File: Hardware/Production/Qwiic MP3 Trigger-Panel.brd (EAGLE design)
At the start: 249.7 x 115.8 mm, 1622 parts, among them J1 MICRO-SD, J104 MICRO-SD, J105 ISP, J106 Poke-Home, J107 3.5mm Audio, J110 PTH, J116 MICRO-SD, J117 ISP, J118 Poke-Home, J119 3.5mm Audio, J122 PTH, J128 MICRO-SD, J129 ISP, J13 PTH, J130 Poke-Home, J131 3.5mm Audio, J134 PTH, J140 MICRO-SD, J141 ISP, J142 Poke-Home, J143 3.5mm Audio, J146 PTH, J152 MICRO-SD, J153 ISP, J154 Poke-Home, J155 3.5mm Audio, J158 PTH, J164 MICRO-SD, J165 ISP, J166 Poke-Home, J167 3.5mm Audio, J170 PTH, J176 MICRO-SD, J177 ISP, J178 Poke-Home, J179 3.5mm Audio, J182 PTH, J188 MICRO-SD, J189 ISP, J190 Poke-Home, J191 3.5mm Audio, J20 MICRO-SD, J21 ISP, J22 Poke-Home, J23 3.5mm Audio, J26 PTH, J3 PTH, J32 MICRO-SD, J33 ISP, J34 Poke-Home, J35 3.5mm Audio, J38 PTH, J44 MICRO-SD, J45 ISP, J46 Poke-Home, J47 3.5mm Audio, J50 PTH, J56 MICRO-SD, J57 ISP, J58 Poke-Home, J59 3.5mm Audio, J62 PTH, J68 MICRO-SD, J69 ISP, J7 ISP, J70 Poke-Home, J71 3.5mm Audio, J74 PTH, J8 3.5mm Audio, J80 MICRO-SD, J81 ISP, J82 Poke-Home, J83 3.5mm Audio, J86 PTH, J9 Poke-Home, J92 MICRO-SD, J93 ISP, J94 Poke-Home, J95 3.5mm Audio, J98 PTH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

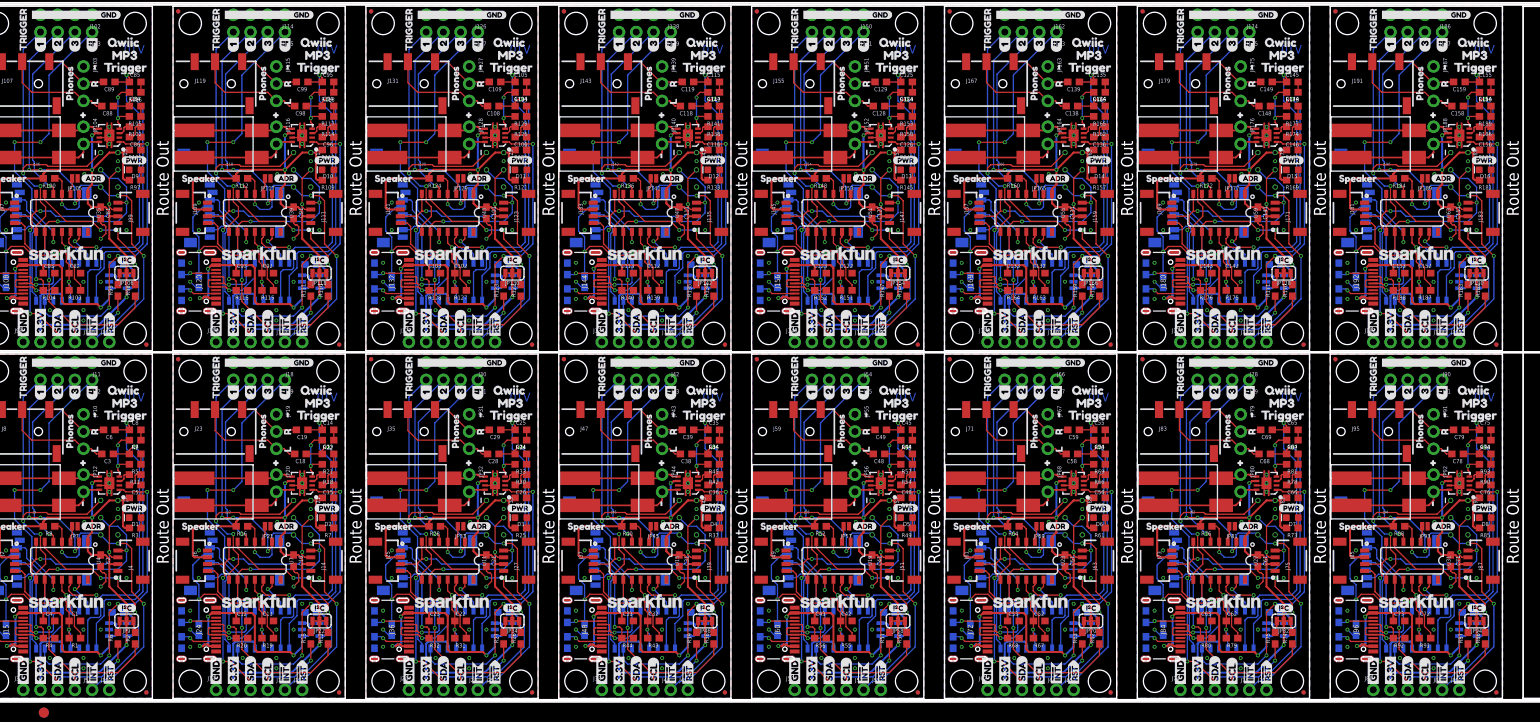
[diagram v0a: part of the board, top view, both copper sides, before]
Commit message: Adding production panel files for v11 reds
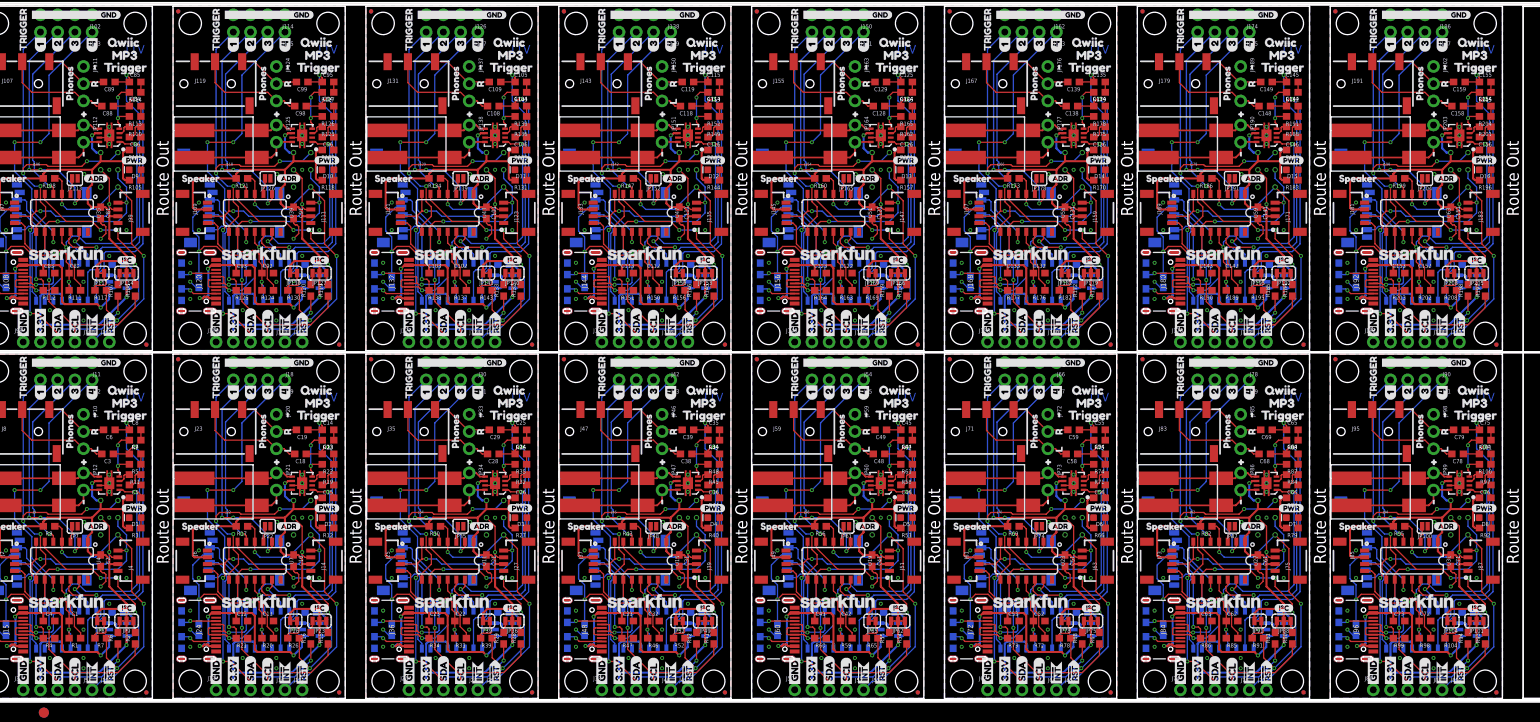
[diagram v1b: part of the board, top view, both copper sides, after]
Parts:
- added JP193, JP194, JP196, JP197, JP206, JP207: STAND-OFF, SparkFun:STAND-OFF
- added JP195, JP208: INT, SparkFun-Jumpers:SMT-JUMPER_2_NC_TRACE_SILK
- added JP198, JP199, JP200, JP201: FIDUCIALUFIDUCIAL, SparkFun:MICRO-FIDUCIAL
- added JP202: PTH, SparkFun-Connectors:1X03_NO_SILK
- added JP203: PTH, SparkFun-Connectors:1X02_NO_SILK
- added JP204: ADR, SparkFun-Jumpers:SMT-JUMPER_2_NO_SILK
- added JP205: (no value), SparkFun-Jumpers:SMT-JUMPER_3_2-NC_TRACE_SILK
- added R193, R194, R206, R207: 5.1k, SparkFun-Resistors:0603
- added R195, R200, R202, R204, R205, R208: 10k, SparkFun-Resistors:0603
- added R196: 1k, SparkFun-Resistors:0603
- added R197, R198, R203: 2.2k, SparkFun-Resistors:0603
- added R199: 4.7k, SparkFun-Resistors:0603
- added R201: 100k, SparkFun-Resistors:0603
- JP100, JP113, JP126, JP87: value FIDUCIALUFIDUCIAL -> ADR; device SparkFun:MICRO-FIDUCIAL -> SparkFun-Jumpers:SMT-JUMPER_2_NO_SILK
- JP101, JP114, JP75, JP88: value FIDUCIALUFIDUCIAL -> (none); device SparkFun:MICRO-FIDUCIAL -> SparkFun-Jumpers:SMT-JUMPER_3_2-NC_TRACE_SILK
- JP102, JP15, JP171, JP183, JP184, JP27, JP28, JP40, JP41, JP51, JP53, JP54, JP63, JP64, JP66, JP76, JP77, JP89, JP90: value FIDUCIALUFIDUCIAL -> STAND-OFF; device SparkFun:MICRO-FIDUCIAL -> SparkFun:STAND-OFF
- JP103, JP115, JP67, JP79: value PTH -> STAND-OFF; device SparkFun-Connectors:1X03_NO_SILK -> SparkFun:STAND-OFF
- JP104: value PTH -> INT; device SparkFun-Connectors:1X02_NO_SILK -> SparkFun-Jumpers:SMT-JUMPER_2_NC_TRACE_SILK
- JP105, JP129, JP141, JP93: value ADR -> STAND-OFF; device SparkFun-Jumpers:SMT-JUMPER_2_NO_NO-SILK -> SparkFun:STAND-OFF
- JP106, JP118, JP142, JP154: value (none) -> STAND-OFF; device SparkFun-Jumpers:SMT-JUMPER_3_2-NC_TRACE_SILK -> SparkFun:STAND-OFF
- JP107, JP108, JP109, JP110, JP120, JP121, JP122, JP133, JP134, JP146, JP71, JP83, JP84, JP95, JP96, JP97: value STAND-OFF -> FIDUCIALUFIDUCIAL; device SparkFun:STAND-OFF -> SparkFun:MICRO-FIDUCIAL
- JP111, JP124, JP137, JP150: value FIDUCIALUFIDUCIAL -> PTH; device SparkFun:MICRO-FIDUCIAL -> SparkFun-Connectors:1X03_NO_SILK
- JP112, JP125, JP138, JP99: value FIDUCIALUFIDUCIAL -> PTH; device SparkFun:MICRO-FIDUCIAL -> SparkFun-Connectors:1X02_NO_SILK
- JP116, JP128, JP80, JP92: value PTH -> STAND-OFF; device SparkFun-Connectors:1X02_NO_SILK -> SparkFun:STAND-OFF
- JP117: value ADR -> INT; device SparkFun-Jumpers:SMT-JUMPER_2_NO_NO-SILK -> SparkFun-Jumpers:SMT-JUMPER_2_NC_TRACE_SILK
- JP127: value PTH -> (none); device SparkFun-Connectors:1X03_NO_SILK -> SparkFun-Jumpers:SMT-JUMPER_3_2-NC_TRACE_SILK
- JP130: value (none) -> INT; device SparkFun-Jumpers:SMT-JUMPER_3_2-NC_TRACE_SILK -> SparkFun-Jumpers:SMT-JUMPER_2_NC_TRACE_SILK
- JP139: value PTH -> ADR; device SparkFun-Connectors:1X03_NO_SILK -> SparkFun-Jumpers:SMT-JUMPER_2_NO_SILK
- JP140: value PTH -> (none); device SparkFun-Connectors:1X02_NO_SILK -> SparkFun-Jumpers:SMT-JUMPER_3_2-NC_TRACE_SILK
- JP143, JP156, JP169, JP182, JP26, JP8: value STAND-OFF -> INT; device SparkFun:STAND-OFF -> SparkFun-Jumpers:SMT-JUMPER_2_NC_TRACE_SILK
- JP151: device SparkFun-Connectors:1X03_NO_SILK -> SparkFun-Connectors:1X02_NO_SILK
- JP152: value PTH -> ADR; device SparkFun-Connectors:1X02_NO_SILK -> SparkFun-Jumpers:SMT-JUMPER_2_NO_SILK
- JP153: value ADR -> (none); device SparkFun-Jumpers:SMT-JUMPER_2_NO_NO-SILK -> SparkFun-Jumpers:SMT-JUMPER_3_2-NC_TRACE_SILK
- JP165, JP7: device SparkFun-Jumpers:SMT-JUMPER_2_NO_NO-SILK -> SparkFun-Jumpers:SMT-JUMPER_2_NO_SILK
- JP175, JP187, JP19, JP31, JP43, JP55: value PTH -> FIDUCIALUFIDUCIAL; device SparkFun-Connectors:1X03_NO_SILK -> SparkFun:MICRO-FIDUCIAL
- JP176, JP20: device SparkFun-Connectors:1X02_NO_SILK -> SparkFun-Connectors:1X03_NO_SILK
- JP177, JP21: value ADR -> PTH; device SparkFun-Jumpers:SMT-JUMPER_2_NO_NO-SILK -> SparkFun-Connectors:1X02_NO_SILK
- JP178, JP22: value (none) -> ADR; device SparkFun-Jumpers:SMT-JUMPER_3_2-NC_TRACE_SILK -> SparkFun-Jumpers:SMT-JUMPER_2_NO_SILK
- JP179, JP192, JP23, JP36, JP49, JP62: value STAND-OFF -> (none); device SparkFun:STAND-OFF -> SparkFun-Jumpers:SMT-JUMPER_3_2-NC_TRACE_SILK
- JP188, JP32, JP44, JP56, JP68: value PTH -> FIDUCIALUFIDUCIAL; device SparkFun-Connectors:1X02_NO_SILK -> SparkFun:MICRO-FIDUCIAL
- JP189, JP33: value ADR -> PTH; device SparkFun-Jumpers:SMT-JUMPER_2_NO_NO-SILK -> SparkFun-Connectors:1X03_NO_SILK
- JP190, JP34: value (none) -> PTH; device SparkFun-Jumpers:SMT-JUMPER_3_2-NC_TRACE_SILK -> SparkFun-Connectors:1X02_NO_SILK
- JP191, JP35, JP48, JP61, JP74: value STAND-OFF -> ADR; device SparkFun:STAND-OFF -> SparkFun-Jumpers:SMT-JUMPER_2_NO_SILK
- JP39, JP52, JP65, JP78: value FIDUCIALUFIDUCIAL -> INT; device SparkFun:MICRO-FIDUCIAL -> SparkFun-Jumpers:SMT-JUMPER_2_NC_TRACE_SILK
- JP45, JP57, JP69, JP81: value ADR -> FIDUCIALUFIDUCIAL; device SparkFun-Jumpers:SMT-JUMPER_2_NO_NO-SILK -> SparkFun:MICRO-FIDUCIAL
- JP46: value (none) -> PTH; device SparkFun-Jumpers:SMT-JUMPER_3_2-NC_TRACE_SILK -> SparkFun-Connectors:1X03_NO_SILK
- JP47, JP60, JP73, JP86: value STAND-OFF -> PTH; device SparkFun:STAND-OFF -> SparkFun-Connectors:1X02_NO_SILK
- JP58, JP70, JP82, JP94: value (none) -> FIDUCIALUFIDUCIAL; device SparkFun-Jumpers:SMT-JUMPER_3_2-NC_TRACE_SILK -> SparkFun:MICRO-FIDUCIAL
- JP59, JP72, JP85, JP98: value STAND-OFF -> PTH; device SparkFun:STAND-OFF -> SparkFun-Connectors:1X03_NO_SILK
- JP91: value PTH -> INT; device SparkFun-Connectors:1X03_NO_SILK -> SparkFun-Jumpers:SMT-JUMPER_2_NC_TRACE_SILK
- R100, R124, R148, R52, R88: value 4.7k -> 10k
- R102, R90: value 100k -> 5.1k
- R103, R115, R129, R141, R142, R154, R77, R89: value 10k -> 5.1k
- R104, R111, R122, R135, R140, R152, R176, R182, R20, R26, R39, R44, R62, R74, R75, R87, R98: value 2.2k -> 10k
- R105, R118, R53, R79: value 10k -> 1k
- R106, R125, R151, R177, R185, R190, R21, R29, R34, R41, R55, R67, R81, R93, R94: value 10k -> 2.2k
- R107, R119, R120, R132, R47, R60: value 5.1k -> 2.2k
- R108, R95: value 5.1k -> 4.7k
- R109, R169, R49, R61, R7, R85: value 1k -> 10k
- R110, R123, R188, R32: value 2.2k -> 100k
- R112, R16, R172, R184, R28: value 4.7k -> 2.2k
- R114, R126, R150, R174, R18, R78: value 100k -> 10k
- R116, R128, R38, R50, R51, R63: value 2.2k -> 5.1k
- R12, R170, R183, R27, R92: value 2.2k -> 1k
- R121: value 1k -> 4.7k
- R131, R144: value 5.1k -> 1k
- R133, R145, R73: value 1k -> 2.2k
- R134, R147, R56: value 2.2k -> 4.7k
- R136: value 4.7k -> 100k
- R138, R42, R54: value 100k -> 2.2k
- R143, R156, R179, R191, R192, R23, R35, R36, R48, R59, R72, R83, R96: value 5.1k -> 10k
- R149, R175, R19, R45, R58: value 10k -> 100k
- R17, R173, R43, R69, R82: value 10k -> 4.7k
- R181, R25, R37: value 1k -> 5.1k
- R186, R30: value 100k -> 4.7k
- R40: value 4.7k -> 1k
- R64, R76: value 4.7k -> 5.1k
- R66: value 100k -> 1k
- R71, R84: value 5.1k -> 100k
- R97: value 1k -> 100k
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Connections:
- new net N$100: C146.2, R188.1
- new net N$101: C144.2, R191.1
- new net N$102: C145.2, R192.1
- new net N$103: J180.B5, R193.2
- new net N$104: J180.A5, R194.2
- new net N$105: JP195.1, R195.2
- new net N$106: D16.A, R196.1
- new net N$107: C156.2, R201.1
- new net N$108: C154.2, R204.1
- new net N$109: C155.2, R205.1
- new net N$110: J192.B5, R206.2
- new net N$111: J192.A5, R207.2
- new net N$112: JP208.1, R208.2
- new net N$97: J168.A5, R181.2
- new net N$98: JP182.1, R182.2
- new net N$99: D15.A, R183.1
- net !INT: now also R7.1
- net !INT1: now also R26.1
- net !INT10: now also R143.1
- net !INT11: now also R156.1
- net !INT12: now also R169.1
- net !INT13: now also R182.1
- net !INT14: now also R195.1
- net !INT15: now also R208.1
- net !INT2: now also R39.1
- net !INT3: now also R52.1
- net !INT4: now also R65.1
- net !INT5: now also R78.1
- net !INT6: now also R91.1
- net !INT7: now also R104.1
- net !INT8: now also R117.1
- net !INT9: now also R130.1
- net !RST1: now also R17.1; no longer R16.1
- net !RST10: now also R134.1; no longer R124.1
- net !RST11: now also R147.1; no longer R136.1
- net !RST12: now also R160.1; no longer R148.1
- net !RST13: now also R173.1; no longer R160.1
- net !RST14: now also R186.1; no longer R172.1
- net !RST15: now also R199.1; no longer R184.1
- net !RST2: now also R30.1; no longer R28.1
- net !RST3: now also R43.1; no longer R40.1
- net !RST4: now also R56.1; no longer R52.1
- net !RST5: now also R69.1; no longer R64.1
- net !RST6: now also R82.1; no longer R76.1
- net !RST7: now also R95.1; no longer R88.1
- net !RST8: now also R108.1; no longer R100.1
- net !RST9: now also R121.1; no longer R112.1
- net !SDN: no longer R10.1, U1.1
- net !SDN1: no longer R17.1, U6.1
- net !SDN10: no longer R125.1, U42.1
- net !SDN11: no longer R137.1, U46.1
- net !SDN12: no longer R149.1, U50.1
- net !SDN13: no longer R161.1, U54.1
- net !SDN14: no longer R173.1, U58.1
- net !SDN15: no longer R185.1, U62.1
- net !SDN2: no longer R29.1, U10.1
- net !SDN3: no longer R41.1, U14.1
- net !SDN4: no longer R53.1, U18.1
- net !SDN5: no longer R65.1, U22.1
- net !SDN6: no longer R77.1, U26.1
- net !SDN7: no longer R89.1, U30.1
- net !SDN8: no longer R101.1, U34.1
- net !SDN9: no longer R113.1, U38.1
- net 3.3V: now also JP8.2
- net 3.3V1: now also JP23.2, JP26.2, R12.2, R18.2; no longer JP22.2, R16.2, R7.2
- net 3.3V10: now also JP140.2, JP143.2, R131.2, R134.2, R135.2; no longer JP130.2, R121.2, R124.2, R125.2
- net 3.3V11: now also JP153.2, JP156.2, R144.2, R147.2, R148.2; no longer JP142.2, R133.2, R136.2, R137.2
- net 3.3V12: now also JP166.2, JP169.2, R157.2, R160.2, R161.2; no longer JP154.2, R145.2, R148.2, R149.2
- net 3.3V13: now also JP179.2, JP182.2, R170.2, R173.2, R174.2; no longer JP166.2, R157.2, R160.2, R161.2
- net 3.3V14: now also JP192.2, JP195.2, R183.2, R186.2, R187.2; no longer JP178.2, R169.2, R172.2, R173.2
- net 3.3V15: now also JP205.2, JP208.2, R196.2, R199.2, R200.2; no longer JP190.2, R181.2, R184.2, R185.2
- net 3.3V2: now also JP36.2, JP39.2, R27.2, R30.2, R31.2; no longer JP34.2, R25.2, R28.2, R29.2
- net 3.3V3: now also JP49.2, JP52.2, R43.2, R44.2; no longer JP46.2, R37.2, R41.2
- net 3.3V4: now also JP62.2, JP65.2, R56.2, R57.2; no longer JP58.2, R49.2, R52.2
- net 3.3V5: now also JP75.2, JP78.2, R66.2, R69.2, R70.2; no longer JP70.2, R61.2, R64.2, R65.2
- net 3.3V6: now also JP88.2, JP91.2, R79.2, R82.2, R83.2; no longer JP82.2, R73.2, R76.2, R77.2
- net 3.3V7: now also JP101.2, JP104.2, R92.2, R95.2, R96.2; no longer JP94.2, R85.2, R88.2, R89.2
- net 3.3V8: now also JP114.2, JP117.2, R105.2, R108.2, R109.2; no longer JP106.2, R100.2, R101.2, R97.2
- net 3.3V9: now also JP127.2, JP130.2, R118.2, R121.2, R122.2; no longer JP118.2, R109.2, R112.2, R113.2
- net AC-L1: now also JP20.3; no longer JP19.3
- net AC-L10: now also JP137.3; no longer JP127.3
- net AC-L11: now also JP150.3; no longer JP139.3
- net AC-L12: now also JP163.3; no longer JP151.3
- net AC-L13: now also JP176.3; no longer JP163.3
- net AC-L14: now also JP189.3; no longer JP175.3
- net AC-L15: now also JP202.3; no longer JP187.3
- net AC-L2: now also JP33.3; no longer JP31.3
- net AC-L3: now also JP46.3; no longer JP43.3
- net AC-L4: now also JP59.3; no longer JP55.3
- net AC-L5: now also JP72.3; no longer JP67.3
- net AC-L6: now also JP85.3; no longer JP79.3
- net AC-L7: now also JP98.3; no longer JP91.3
- net AC-L8: now also JP111.3; no longer JP103.3
- net AC-L9: now also JP124.3; no longer JP115.3
- net AC-R1: now also JP20.2; no longer JP19.2
- net AC-R10: now also JP137.2; no longer JP127.2
- net AC-R11: now also JP150.2; no longer JP139.2
- net AC-R12: now also JP163.2; no longer JP151.2
- net AC-R13: now also JP176.2; no longer JP163.2
- net AC-R14: now also JP189.2; no longer JP175.2
- net AC-R15: now also JP202.2; no longer JP187.2
- net AC-R2: now also JP33.2; no longer JP31.2
- net AC-R3: now also JP46.2; no longer JP43.2
- net AC-R4: now also JP59.2; no longer JP55.2
- net AC-R5: now also JP72.2; no longer JP67.2
- net AC-R6: now also JP85.2; no longer JP79.2
- net AC-R7: now also JP98.2; no longer JP91.2
- net AC-R8: now also JP111.2; no longer JP103.2
- net AC-R9: now also JP124.2; no longer JP115.2
- net ADKEY1: now also R20.1; no longer R19.1
- net ADKEY10: now also R137.1; no longer R127.1
- net ADKEY11: now also R150.1; no longer R139.1
- net ADKEY12: now also R163.1; no longer R151.1
- net ADKEY13: now also R176.1; no longer R163.1
- net ADKEY14: now also R189.1; no longer R175.1
- net ADKEY15: now also R202.1; no longer R187.1
- net ADKEY2: now also R33.1; no longer R31.1
- net ADKEY3: now also R46.1; no longer R43.1
- net ADKEY4: now also R59.1; no longer R55.1
- net ADKEY5: now also R72.1; no longer R67.1
- net ADKEY6: now also R85.1; no longer R79.1
- net ADKEY7: now also R98.1; no longer R91.1
- net ADKEY8: now also R111.1; no longer R103.1
- net ADKEY9: now also R124.1; no longer R115.1
- net ADR1: now also JP22.2; no longer JP21.2
- net ADR10: now also JP139.2; no longer JP129.2
- net ADR11: now also JP152.2; no longer JP141.2
- net ADR12: now also JP165.2; no longer JP153.2
- net ADR13: now also JP178.2; no longer JP165.2
- net ADR14: now also JP191.2; no longer JP177.2
- net ADR15: now also JP204.2; no longer JP189.2
- net ADR2: now also JP35.2; no longer JP33.2
- net ADR3: now also JP48.2; no longer JP45.2
- net ADR4: now also JP61.2; no longer JP57.2
- net ADR5: now also JP74.2; no longer JP69.2
- net ADR6: now also JP87.2; no longer JP81.2
- net ADR7: now also JP100.2; no longer JP93.2
- net ADR8: now also JP113.2; no longer JP105.2
- net ADR9: now also JP126.2; no longer JP117.2
- net GND1: now also JP20.1, JP22.1, R21.1, R25.1; no longer JP19.1, JP21.1, R20.1, R23.1
- net GND10: now also JP137.1, JP139.1, R138.1, R141.1, R142.1; no longer JP127.1, JP129.1, R128.1, R131.1, R132.1
- net GND11: now also JP150.1, JP152.1, R151.1, R154.1, R155.1; no longer JP139.1, JP141.1, R140.1, R143.1, R144.1
- net GND12: now also JP163.1, JP165.1, R164.1, R167.1, R168.1; no longer JP151.1, JP153.1, R152.1, R155.1, R156.1
- net GND13: now also JP176.1, JP178.1, R177.1, R180.1, R181.1; no longer JP163.1, JP165.1, R164.1, R167.1, R168.1
- net GND14: now also JP189.1, JP191.1, R190.1, R193.1, R194.1; no longer JP175.1, JP177.1, R176.1, R179.1, R180.1
- net GND15: now also JP202.1, JP204.1, R203.1, R206.1, R207.1; no longer JP187.1, JP189.1, R188.1, R191.1, R192.1
- net GND2: now also JP35.1, R34.1, R37.1, R38.1; no longer JP31.1, R32.1, R35.1, R36.1
- net GND3: now also JP46.1, JP48.1, R50.1, R51.1; no longer JP43.1, JP45.1, R44.1, R48.1
- net GND4: now also JP59.1, JP61.1, R63.1, R64.1; no longer JP55.1, JP57.1, R56.1, R59.1
- net GND5: now also JP72.1, JP74.1, R73.1, R76.1, R77.1; no longer JP67.1, JP69.1, R68.1, R71.1, R72.1
- net GND6: now also JP85.1, JP87.1, R86.1, R89.1, R90.1; no longer JP79.1, JP81.1, R80.1, R83.1, R84.1
- net GND7: now also JP100.1, JP98.1, R102.1, R103.1, R99.1; no longer JP91.1, JP93.1, R92.1, R95.1, R96.1
- net GND8: now also JP111.1, JP113.1, R112.1, R115.1, R116.1; no longer JP103.1, JP105.1, R104.1, R107.1, R108.1
- net GND9: now also JP124.1, JP126.1, R125.1, R128.1, R129.1; no longer JP115.1, JP117.1, R116.1, R119.1, R120.1
- net IN+AMP1: now also R19.2; no longer R18.2
- net IN+AMP10: now also R136.2; no longer R126.2
- net IN+AMP11: now also R149.2; no longer R138.2
- net IN+AMP12: now also R162.2; no longer R150.2
- net IN+AMP13: now also R175.2; no longer R162.2
- net IN+AMP14: now also R188.2; no longer R174.2
- net IN+AMP15: now also R201.2; no longer R186.2
- net IN+AMP2: now also R32.2; no longer R30.2
- net IN+AMP3: now also R45.2; no longer R42.2
- net IN+AMP4: now also R58.2; no longer R54.2
- net IN+AMP5: now also R71.2; no longer R66.2
- net IN+AMP6: now also R84.2; no longer R78.2
- net IN+AMP7: now also R97.2; no longer R90.2
- net IN+AMP8: now also R110.2; no longer R102.2
- net IN+AMP9: now also R123.2; no longer R114.2
- net IN-AMP1: now also R23.2; no longer R21.2
- net IN-AMP10: now also R139.2, R140.2; no longer R129.2, R130.2
- net IN-AMP11: now also R152.2, R153.2; no longer R141.2, R142.2
- net IN-AMP12: now also R165.2, R166.2; no longer R153.2, R154.2
- net IN-AMP13: now also R178.2, R179.2; no longer R165.2, R166.2
- net IN-AMP14: now also R191.2, R192.2; no longer R177.2, R178.2
- net IN-AMP15: now also R204.2, R205.2; no longer R189.2, R190.2
- net IN-AMP2: now also R35.2, R36.2; no longer R33.2, R34.2
- net IN-AMP3: now also R48.2, R49.2; no longer R45.2, R46.2
- net IN-AMP4: now also R61.2, R62.2; no longer R57.2, R58.2
- net IN-AMP5: now also R74.2, R75.2; no longer R69.2, R70.2
- net IN-AMP6: now also R87.2, R88.2; no longer R81.2, R82.2
- net IN-AMP7: now also R100.2, R101.2; no longer R93.2, R94.2
- net IN-AMP8: now also R113.2, R114.2; no longer R105.2, R106.2
- net IN-AMP9: now also R126.2, R127.2; no longer R117.2, R118.2
- net N$10: now also C13.2; no longer C14.2
- net N$11: now also C14.2, R23.1; no longer J24.B5, R23.2
- net N$12: now also J24.B5; no longer J24.A5
- net N$13: now also J24.A5, R25.2; no longer D3.A, R25.1
- net N$14: now also JP26.1, R26.2; no longer C26.2, R30.1
- net N$15: now also D3.A, R27.1; no longer C24.2, R33.1
- net N$16: now also C26.2, R32.1; no longer C25.2, R34.1
- net N$17: now also C24.2, R35.1; no longer J36.B5, R35.2
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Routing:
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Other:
- board text added: "V11"
- board text removed: "V10"

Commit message: Re-route to accommodate H4
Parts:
- removed C100, C103, C106, C107, C110, C113, C116, C117, C120, C123, C126, C127, C130, C133, C136, C137, C140, C143, C146, C147, C150, C153, C156, C157, C160, C63, C66, C67, C70, C73, C76, C77, C80, C83, C86, C87, C90, C93, C96, C97: 1.0uF, SparkFun-Capacitors:0603
- removed C101, C104, C105, C111, C114, C115, C121, C124, C125, C131, C134, C135, C141, C144, C145, C151, C154, C155, C61, C64, C65, C71, C74, C75, C81, C84, C85, C91, C94, C95: 0.1uF, SparkFun-Capacitors:0603
- removed C102, C112, C122, C132, C142, C152, C62, C72, C82, C92: 10uF, SparkFun-Capacitors:0603
- removed C108, C109, C118, C119, C128, C129, C138, C139, C148, C149, C158, C159, C68, C69, C78, C79, C88, C89, C98, C99: 0.22uF, SparkFun-Capacitors:0603
- removed D10, D11, D12, D13, D14, D15, D16, D7, D8, D9: RED, SparkFun-LED:LED-0603
- removed J100, J101, J112, J113, J124, J125, J136, J137, J148, J149, J160, J161, J172, J173, J184, J185, J76, J77, J88, J89: (no value), SparkFun-Connectors:1X01_NO_SILK
- removed J102, J103, J114, J115, J126, J127, J138, J139, J150, J151, J162, J163, J174, J175, J186, J187, J78, J79, J90, J91: (no value), SparkFun-Connectors:1X04_NO_SILK
- removed J104, J116, J128, J140, J152, J164, J176, J188, J80, J92: MICRO-SD, SparkFun-Connectors:MICRO-SD-SOCKET
- removed J105, J117, J129, J141, J153, J165, J177, J189, J81, J93: ISP, SparkFun-Connectors:2X3_TEST_POINTS
- removed J106, J118, J130, J142, J154, J166, J178, J190, J82, J94: Poke-Home, SparkFun-Connectors:1X02_POKEHOME
- removed J107, J119, J131, J143, J155, J167, J179, J191, J83, J95: 3.5mm Audio, SparkFun-Connectors:AUDIO_JACK_3.5MM_TRRS_SMD_RA
- removed J108, J120, J132, J144, J156, J168, J180, J192, J84, J96: (no value), SparkFun-Connectors:USB-C-16P
- removed J109, J111, J121, J123, J133, J135, J145, J147, J157, J159, J169, J171, J181, J183, J73, J75, J85, J87, J97, J99: (no value), SparkFun-Connectors:1X04_1MM_RA
- removed J110, J122, J134, J146, J158, J170, J182, J74, J86, J98: PTH, SparkX:1X04_NO_SILK
- removed JP100, JP113, JP126, JP139, JP152, JP165, JP178, JP191, JP204, JP87: ADR, SparkFun-Jumpers:SMT-JUMPER_2_NO_SILK
- removed JP101, JP114, JP127, JP140, JP153, JP166, JP179, JP192, JP205, JP88: (no value), SparkFun-Jumpers:SMT-JUMPER_3_2-NC_TRACE_SILK
- removed JP102, JP103, JP105, JP106, JP115, JP116, JP118, JP119, JP128, JP129, JP131, JP132, JP141, JP142, JP144, JP145, JP154, JP155, JP157, JP158, JP167, JP168, JP170, JP171, JP180, JP181, JP183, JP184, JP193, JP194, JP196, JP197, JP206, JP207, JP89, JP90, JP92, JP93: STAND-OFF, SparkFun:STAND-OFF
- removed JP104, JP117, JP130, JP143, JP156, JP169, JP182, JP195, JP208, JP91: INT, SparkFun-Jumpers:SMT-JUMPER_2_NC_TRACE_SILK
- removed JP107, JP108, JP109, JP110, JP120, JP121, JP122, JP123, JP133, JP134, JP135, JP136, JP146, JP147, JP148, JP149, JP159, JP160, JP161, JP162, JP172, JP173, JP174, JP175, JP185, JP186, JP187, JP188, JP198, JP199, JP200, JP201, JP94, JP95, JP96, JP97: FIDUCIALUFIDUCIAL, SparkFun:MICRO-FIDUCIAL
- removed JP111, JP124, JP137, JP150, JP163, JP176, JP189, JP202, JP85, JP98: PTH, SparkFun-Connectors:1X03_NO_SILK
- removed JP112, JP125, JP138, JP151, JP164, JP177, JP190, JP203, JP86, JP99: PTH, SparkFun-Connectors:1X02_NO_SILK
- removed LOGO19, LOGO22, LOGO25, LOGO28, LOGO31, LOGO34, LOGO37, LOGO40, LOGO43, LOGO46: OSHW-LOGOMINI, SparkFun-Aesthetics:OSHW-LOGO-MINI
- removed LOGO20, LOGO23, LOGO26, LOGO29, LOGO32, LOGO35, LOGO38, LOGO41, LOGO44, LOGO47: SFE_LOGO_NAME.1_INCH, SparkFun-Aesthetics:SFE_LOGO_NAME_.1
- removed LOGO21, LOGO24, LOGO27, LOGO30, LOGO33, LOGO36, LOGO39, LOGO42, LOGO45, LOGO48: SFE_LOGO_NAME_FLAME.1_INCH, SparkFun-Aesthetics:SFE_LOGO_NAME_FLAME_.1
- removed R100, R101, R104, R109, R111, R113, R114, R117, R122, R124, R126, R127, R130, R135, R137, R139, R140, R143, R148, R150, R152, R153, R156, R161, R163, R165, R166, R169, R174, R176, R178, R179, R182, R187, R189, R191, R192, R195, R200, R202, R204, R205, R208, R83, R85, R87, R88, R91, R96, R98: 10k, SparkFun-Resistors:0603
- removed R102, R103, R115, R116, R128, R129, R141, R142, R154, R155, R167, R168, R180, R181, R193, R194, R206, R207, R89, R90: 5.1k, SparkFun-Resistors:0603
- removed R105, R118, R131, R144, R157, R170, R183, R196, R79, R92: 1k, SparkFun-Resistors:0603
- removed R106, R107, R112, R119, R120, R125, R132, R133, R138, R145, R146, R151, R158, R159, R164, R171, R172, R177, R184, R185, R190, R197, R198, R203, R80, R81, R86, R93, R94, R99: 2.2k, SparkFun-Resistors:0603
- removed R108, R121, R134, R147, R160, R173, R186, R199, R82, R95: 4.7k, SparkFun-Resistors:0603
- removed R110, R123, R136, R149, R162, R175, R188, R201, R84, R97: 100k, SparkFun-Resistors:0603
- removed U$289, U$333, U$336, U$380, U$383, U$427, U$430, U$474, U$477, U$521, U$524, U$568, U$571, U$615, U$618, U$662, U$665, U$709, U$712: (no value), Labels-0_04:SDA8
- removed U$290, U$332, U$337, U$379, U$384, U$426, U$431, U$473, U$478, U$520, U$525, U$567, U$572, U$614, U$619, U$661, U$666, U$708, U$713: (no value), Labels-0_04:SCL9
- removed U$291, U$338, U$385, U$432, U$479, U$526, U$573, U$620, U$667, U$714: (no value), Labels:I_SUPER2_C-()-03
- removed U$292, U$293, U$339, U$340, U$386, U$387, U$433, U$434, U$480, U$481, U$527, U$528, U$574, U$575, U$621, U$622, U$668, U$669, U$715, U$716: (no value), Labels:INT#-[<
- removed U$294, U$295, U$341, U$342, U$388, U$389, U$435, U$436, U$482, U$483, U$529, U$530, U$576, U$577, U$623, U$624, U$670, U$671, U$717, U$718: (no value), Labels:RST#-[>
- removed U$296, U$343, U$390, U$437, U$484, U$531, U$578, U$625, U$672, U$719: (no value), Labels:PWR-()-03
- removed U$297, U$344, U$391, U$438, U$485, U$532, U$579, U$626, U$673, U$720: (no value), Labels:ADR-()-03
- removed U$298, U$321, U$345, U$368, U$392, U$415, U$439, U$462, U$486, U$509, U$533, U$556, U$580, U$603, U$627, U$650, U$674, U$697, U$721, U$744: (no value), buzzard_labels (13):TRIGGER5
- removed U$299, U$319, U$346, U$366, U$393, U$413, U$440, U$460, U$487, U$507, U$534, U$554, U$581, U$601, U$628, U$648, U$675, U$695, U$722, U$742: (no value), buzzard_labels (14):21
- removed U$300, U$315, U$347, U$362, U$394, U$409, U$441, U$456, U$488, U$503, U$535, U$550, U$582, U$597, U$629, U$644, U$676, U$691, U$723, U$738: (no value), buzzard_labels (14):32
- removed U$301, U$314, U$348, U$361, U$395, U$408, U$442, U$455, U$489, U$502, U$536, U$549, U$583, U$596, U$630, U$643, U$677, U$690, U$724, U$737: (no value), buzzard_labels (14):43
- removed U$302, U$313, U$349, U$360, U$396, U$407, U$443, U$454, U$490, U$501, U$537, U$548, U$584, U$595, U$631, U$642, U$678, U$689, U$725, U$736: (no value), buzzard_labels (16):#5
- removed U$303, U$308, U$312, U$316, U$350, U$355, U$359, U$363, U$397, U$402, U$406, U$410, U$444, U$449, U$453, U$457, U$491, U$496, U$500, U$504, U$538, U$543, U$547, U$551, U$585, U$590, U$594, U$598, U$632, U$637, U$641, U$645, U$679, U$684, U$688, U$692, U$726, U$731, U$735, U$739: (no value), buzzard_labels (16):#6
- removed U$304, U$320, U$351, U$367, U$398, U$414, U$445, U$461, U$492, U$508, U$539, U$555, U$586, U$602, U$633, U$649, U$680, U$696, U$727, U$743: (no value), buzzard_labels (16):1_1
- removed U$305, U$322, U$352, U$369, U$399, U$416, U$446, U$463, U$493, U$510, U$540, U$557, U$587, U$604, U$634, U$651, U$681, U$698, U$728, U$745: (no value), buzzard_labels (16):GND0
- removed U$306, U$318, U$353, U$365, U$400, U$412, U$447, U$459, U$494, U$506, U$541, U$553, U$588, U$600, U$635, U$647, U$682, U$694, U$729, U$741: (no value), buzzard_labels (16):L12
- removed U$307, U$317, U$354, U$364, U$401, U$411, U$448, U$458, U$495, U$505, U$542, U$552, U$589, U$599, U$636, U$646, U$683, U$693, U$730, U$740: (no value), buzzard_labels (16):R11
- removed U$309, U$323, U$356, U$370, U$403, U$417, U$450, U$464, U$497, U$511, U$544, U$558, U$591, U$605, U$638, U$652, U$685, U$699, U$732, U$746: (no value), buzzard_labels (17):PHONES0
- removed U$310, U$324, U$357, U$371, U$404, U$418, U$451, U$465, U$498, U$512, U$545, U$559, U$592, U$606, U$639, U$653, U$686, U$700, U$733, U$747: (no value), buzzard_labels (17):SPEAKER1
- removed U$311, U$358, U$405, U$452, U$499, U$546, U$593, U$640, U$687, U$734: (no value), buzzard_labels (17):QWIIC_MP32
- removed U$325, U$372, U$419, U$466, U$513, U$560, U$607, U$654, U$701, U$748: (no value), Labels:QWIIC-LOGO-MEDIUM
- removed U$326, U$373, U$420, U$467, U$514, U$561, U$608, U$655, U$702, U$749: (no value), buzzard_labels (2):TRIGGER4
- removed U$327, U$374, U$421, U$468, U$515, U$562, U$609, U$656, U$703, U$750: (no value), buzzard_labels (3):MP31
- removed U$328, U$375, U$422, U$469, U$516, U$563, U$610, U$657, U$704, U$751: (no value), buzzard_labels (3):QWIIC0
- removed U$329, U$376, U$423, U$470, U$517, U$564, U$611, U$658, U$705, U$752: (no value), buzzard_labels (3):TRIGGER2
- removed U$330, U$335, U$377, U$382, U$424, U$429, U$471, U$476, U$518, U$523, U$565, U$570, U$612, U$617, U$659, U$664, U$706, U$711: (no value), Labels-0_04:3#3V2
- removed U$331, U$334, U$378, U$381, U$425, U$428, U$472, U$475, U$519, U$522, U$566, U$569, U$613, U$616, U$660, U$663, U$707, U$710: (no value), Labels-0_04:GND1
- removed U25, U29, U33, U37, U41, U45, U49, U53, U57, U61: WT2003S, WT2003S:SO16
- removed U26, U30, U34, U38, U42, U46, U50, U54, U58, U62: TPA2005D1, SparkFun-IC-Amplifiers:QFN-8_PAD
- removed U27, U31, U35, U39, U43, U47, U51, U55, U59, U63: ATTINY84-ARDUINO, SparkFun-IC-Microcontroller:SO14
- removed U28, U32, U36, U40, U44, U48, U52, U56, U60, U64: AP2112-3.3V, SparkFun-PowerIC:SOT23-5
- J14, J2, J25, J27, J37, J39, J4, J49, J51, J6, J61, J63: value (none) -> QWIIC_RIGHT_ANGLE; device SparkFun-Connectors:1X04_1MM_RA -> SparkFun-Connectors:JST04_1MM_RA
- J15, J24, J36, J48, J60, J72: device SparkFun-Connectors:USB-C-16P -> SparkFun-Connectors:USB-C-16P-2LAYER-PADS
- JP14, JP28: value STAND-OFF -> JUMPER-SMT_2_NC_TRACE_SILK; device SparkFun:STAND-OFF -> SparkFun-Jumpers:SMT-JUMPER_2_NC_TRACE_SILK
- JP16, JP29, JP30, JP43, JP44, JP57, JP58, JP68, JP71, JP81, JP82: value FIDUCIALUFIDUCIAL -> STAND-OFF; device SparkFun:MICRO-FIDUCIAL -> SparkFun:STAND-OFF
- JP20, JP33, JP46, JP59: value PTH -> FIDUCIALUFIDUCIAL; device SparkFun-Connectors:1X03_NO_SILK -> SparkFun:MICRO-FIDUCIAL
- JP21: device SparkFun-Connectors:1X02_NO_SILK -> SparkFun-Connectors:1X03_NO_SILK
- JP22: value ADR -> PTH; device SparkFun-Jumpers:SMT-JUMPER_2_NO_SILK -> SparkFun-Connectors:1X02_NO_SILK
- JP23: value (none) -> ADR; device SparkFun-Jumpers:SMT-JUMPER_3_2-NC_TRACE_SILK -> SparkFun-Jumpers:SMT-JUMPER_2_NO_SILK
- JP24, JP38, JP66, JP80: value STAND-OFF -> JUMPER-SMT_3_2-NC_TRACE_SILK; device SparkFun:STAND-OFF -> SparkFun-Jumpers:SMT-JUMPER_3_2-NC_TRACE_SILK
- JP26, JP39: value INT -> STAND-OFF; device SparkFun-Jumpers:SMT-JUMPER_2_NC_TRACE_SILK -> SparkFun:STAND-OFF
- JP27, JP41: value STAND-OFF -> INT; device SparkFun:STAND-OFF -> SparkFun-Jumpers:SMT-JUMPER_2_NC_TRACE_SILK
- JP34, JP47, JP60, JP73: value PTH -> FIDUCIALUFIDUCIAL; device SparkFun-Connectors:1X02_NO_SILK -> SparkFun:MICRO-FIDUCIAL
- JP35: value ADR -> PTH; device SparkFun-Jumpers:SMT-JUMPER_2_NO_SILK -> SparkFun-Connectors:1X03_NO_SILK
- JP36: value (none) -> PTH; device SparkFun-Jumpers:SMT-JUMPER_3_2-NC_TRACE_SILK -> SparkFun-Connectors:1X02_NO_SILK
- JP37, JP51, JP79: value STAND-OFF -> ADR; device SparkFun:STAND-OFF -> SparkFun-Jumpers:SMT-JUMPER_2_NO_SILK
- JP42, JP56, JP70, JP84: value FIDUCIALUFIDUCIAL -> JUMPER-SMT_2_NC_TRACE_SILK; device SparkFun:MICRO-FIDUCIAL -> SparkFun-Jumpers:SMT-JUMPER_2_NC_TRACE_SILK
- JP48, JP61, JP74: value ADR -> FIDUCIALUFIDUCIAL; device SparkFun-Jumpers:SMT-JUMPER_2_NO_SILK -> SparkFun:MICRO-FIDUCIAL
- JP49: value (none) -> PTH; device SparkFun-Jumpers:SMT-JUMPER_3_2-NC_TRACE_SILK -> SparkFun-Connectors:1X03_NO_SILK
- JP50, JP64: value STAND-OFF -> PTH; device SparkFun:STAND-OFF -> SparkFun-Connectors:1X02_NO_SILK
- JP52: value INT -> JUMPER-SMT_3_2-NC_TRACE_SILK; device SparkFun-Jumpers:SMT-JUMPER_2_NC_TRACE_SILK -> SparkFun-Jumpers:SMT-JUMPER_3_2-NC_TRACE_SILK
- JP55, JP69, JP83: value FIDUCIALUFIDUCIAL -> INT; device SparkFun:MICRO-FIDUCIAL -> SparkFun-Jumpers:SMT-JUMPER_2_NC_TRACE_SILK
- JP62, JP75: value (none) -> FIDUCIALUFIDUCIAL; device SparkFun-Jumpers:SMT-JUMPER_3_2-NC_TRACE_SILK -> SparkFun:MICRO-FIDUCIAL
- JP63, JP77: value STAND-OFF -> PTH; device SparkFun:STAND-OFF -> SparkFun-Connectors:1X03_NO_SILK
- JP65: value INT -> ADR; device SparkFun-Jumpers:SMT-JUMPER_2_NC_TRACE_SILK -> SparkFun-Jumpers:SMT-JUMPER_2_NO_SILK
- JP72: value PTH -> STAND-OFF; device SparkFun-Connectors:1X03_NO_SILK -> SparkFun:STAND-OFF
- JP76: value STAND-OFF -> FIDUCIALUFIDUCIAL; device SparkFun:STAND-OFF -> SparkFun:MICRO-FIDUCIAL
- JP78: value INT -> PTH; device SparkFun-Jumpers:SMT-JUMPER_2_NC_TRACE_SILK -> SparkFun-Connectors:1X02_NO_SILK
- JP9: value (none) -> JUMPER-SMT_3_2-NC_TRACE_SILK
- U$100: device Labels-0_04:3#3V2 -> Labels-0_04:SDA8
- U$101, U$242, U$98: device Labels-0_04:SDA8 -> Labels-0_04:GND1
- U$102, U$97: device Labels-0_04:SCL9 -> Labels-0_04:3#3V2
- U$103, U$244: device Labels:I_SUPER2_C-()-03 -> Labels-0_04:SDA8
- U$104, U$152: device Labels:INT#-[< -> Labels-0_04:SCL9
- U$105, U$57: device Labels:INT#-[< -> Labels:I_SUPER2_C-()-03
- U$106, U$107, U$154, U$59: device Labels:RST#-[> -> Labels:INT#-[<
- U$108, U$61: device Labels:PWR-()-03 -> Labels:RST#-[>
- U$109, U$156: device Labels:ADR-()-03 -> Labels:RST#-[>
- U$110: device buzzard_labels (13):TRIGGER5 -> Labels:PWR-()-03
- U$111: device buzzard_labels (14):21 -> Labels:ADR-()-03
- U$112: device buzzard_labels (14):32 -> buzzard_labels (13):TRIGGER5
- U$113: device buzzard_labels (14):43 -> buzzard_labels (14):21
- U$114: device buzzard_labels (16):#5 -> buzzard_labels (14):32
- U$115, U$128: device buzzard_labels (16):#6 -> buzzard_labels (14):43
- U$116: device buzzard_labels (16):1_1 -> buzzard_labels (16):#5
- U$117: device buzzard_labels (16):GND0 -> buzzard_labels (16):#6
- U$118: device buzzard_labels (16):L12 -> buzzard_labels (16):1_1
- U$119: device buzzard_labels (16):R11 -> buzzard_labels (16):GND0
- U$120: device buzzard_labels (16):#6 -> buzzard_labels (16):L12
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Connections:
- removed net !INT10: J124.1, R143.1, U43.6
- removed net !INT11: J136.1, R156.1, U47.6
- removed net !INT12: J148.1, R169.1, U51.6
- removed net !INT13: J160.1, R182.1, U55.6
- removed net !INT14: J172.1, R195.1, U59.6
- removed net !INT15: J184.1, R208.1, U63.6
- removed net !INT6: J76.1, R91.1, U27.6
- removed net !INT7: J88.1, R104.1, U31.6
- removed net !INT8: J100.1, R117.1, U35.6
- removed net !INT9: J112.1, R130.1, U39.6
- removed net !RST10: J125.1, J129.5, R134.1, U43.4
- removed net !RST11: J137.1, J141.5, R147.1, U47.4
- removed net !RST12: J149.1, J153.5, R160.1, U51.4
- removed net !RST13: J161.1, J165.5, R173.1, U55.4
- removed net !RST14: J173.1, J177.5, R186.1, U59.4
- removed net !RST15: J185.1, J189.5, R199.1, U63.4
- removed net !RST6: J77.1, J81.5, R82.1, U27.4
- removed net !RST7: J89.1, J93.5, R95.1, U31.4
- removed net !RST8: J101.1, J105.5, R108.1, U35.4
- removed net !RST9: J113.1, J117.5, R121.1, U39.4
- removed net !SDN: U2.7
- removed net !SDN1: U5.7
- removed net !SDN10: U41.7
- removed net !SDN11: U45.7
- removed net !SDN12: U49.7
- removed net !SDN13: U53.7
- removed net !SDN14: U57.7
- removed net !SDN15: U61.7
- removed net !SDN2: U9.7
- removed net !SDN3: U13.7
- removed net !SDN4: U17.7
- removed net !SDN5: U21.7
- removed net !SDN6: U25.7
- removed net !SDN7: U29.7
- removed net !SDN8: U33.7
- removed net !SDN9: U37.7
- removed net 3.3V10: C101.1, C107.1, J121.2, J122.2, J123.2, J129.2, JP140.2, JP143.2, R131.2, R134.2, R135.2, U41.5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
- removed net 3.3V11: C111.1, C117.1, J133.2, J134.2, J135.2, J141.2, JP153.2, JP156.2, R144.2, R147.2, R148.2, U45.5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
- removed net 3.3V12: C121.1, C127.1, J145.2, J146.2, J147.2, J153.2, JP166.2, JP169.2, R157.2, R160.2, R161.2, U49.5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
- removed net 3.3V13: C131.1, C137.1, J157.2, J158.2, J159.2, J165.2, JP179.2, JP182.2, R170.2, R173.2, R174.2, U53.5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
- removed net 3.3V14: C141.1, C147.1, J169.2, J170.2, J171.2, J177.2, JP192.2, JP195.2, R183.2, R186.2, R187.2, U57.5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
- removed net 3.3V15: C151.1, C157.1, J181.2, J182.2, J183.2, J189.2, JP205.2, JP208.2, R196.2, R199.2, R200.2, U61.5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
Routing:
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- removed copper zone on layer 1, net GND10
- removed copper zone on layer 16, net GND10
- removed copper zone on layer 1, net GND11
- removed copper zone on layer 16, net GND11
- removed copper zone on layer 1, net GND12
- removed copper zone on layer 16, net GND12
- removed copper zone on layer 1, net GND13
- removed copper zone on layer 16, net GND13
- removed copper zone on layer 1, net GND14
- removed copper zone on layer 16, net GND14
- removed copper zone on layer 1, net GND15
- removed copper zone on layer 16, net GND15
- removed copper zone on layer 1, net GND6
- removed copper zone on layer 16, net GND6
- removed copper zone on layer 1, net GND7
- removed copper zone on layer 16, net GND7
- removed copper zone on layer 1, net GND8
- removed copper zone on layer 16, net GND8
- removed copper zone on layer 1, net GND9
- removed copper zone on layer 16, net GND9
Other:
- board size 249.7 x 115.8 mm -> 115.6 x 115.8 mm
- board text added: "v20"
- board text removed: "V11"

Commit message: v20 small test panel
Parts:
- C13, C14, C24, C25, C34, C35, C44, C45, C54, C55, C7, C8: value 0.1uF -> 10nF
- C15, C26, C36, C46, C5, C56: value 1.0uF -> 22nF; device SparkFun-Capacitors:0603 -> SparkFun-Capacitors:0402
- R11, R19, R32, R45, R58, R71: value 100k -> 47k
- R17, R30, R43, R56, R69, R8: value 4.7k -> 10k
- R22, R23, R35, R36, R48, R49, R5, R61, R62, R74, R75, R9: value 10k -> 100k
- moved U10 0.64 mm to (73.0, 20.3)
- moved U18 0.64 mm to (42.5, 71.6)
- moved U22 0.64 mm to (73.0, 71.6)
- moved U6 0.64 mm to (42.5, 20.3)
- moved U14 0.63 mm to (12.1, 71.6)
- moved U4 0.63 mm to (12.1, 20.3)
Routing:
- net !RST2: track 41.3 -> 42.2 mm
- net !RST1: track 41.3 -> 42.2 mm
- net !RST5: track 41.3 -> 42.2 mm
- net !RST4: track 41.3 -> 42.2 mm
- net !RST3: track 41.3 -> 42.2 mm
- net !RST: track 41.3 -> 42.2 mm
- net TRIGGER22: track 48.7 -> 47.9 mm
- net TRIGGER10: track 48.7 -> 47.9 mm
- net TRIGGER1: track 48.7 -> 47.9 mm
- net TRIGGER6: track 48.7 -> 47.9 mm
- net TRIGGER18: track 48.7 -> 47.9 mm
- net TRIGGER14: track 48.7 -> 47.9 mm
- net 3.3V3: track 94.9 -> 94.2 mm
- net 3.3V2: track 94.9 -> 94.2 mm
- net 3.3V: track 94.9 -> 94.2 mm
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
